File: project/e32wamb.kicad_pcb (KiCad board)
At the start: 2 copper layers, 50 x 37 mm, 34 parts, among them J1 2059-302_998-403, J2 Conn_01x04, J3 Conn_01x03, Q1 AO3400, Q2 AO3400, Q3 AO3400, Q4 AO3400, Q5 AO3400, SW1 TS-1187A-B-A-B, U1 AP63203WU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

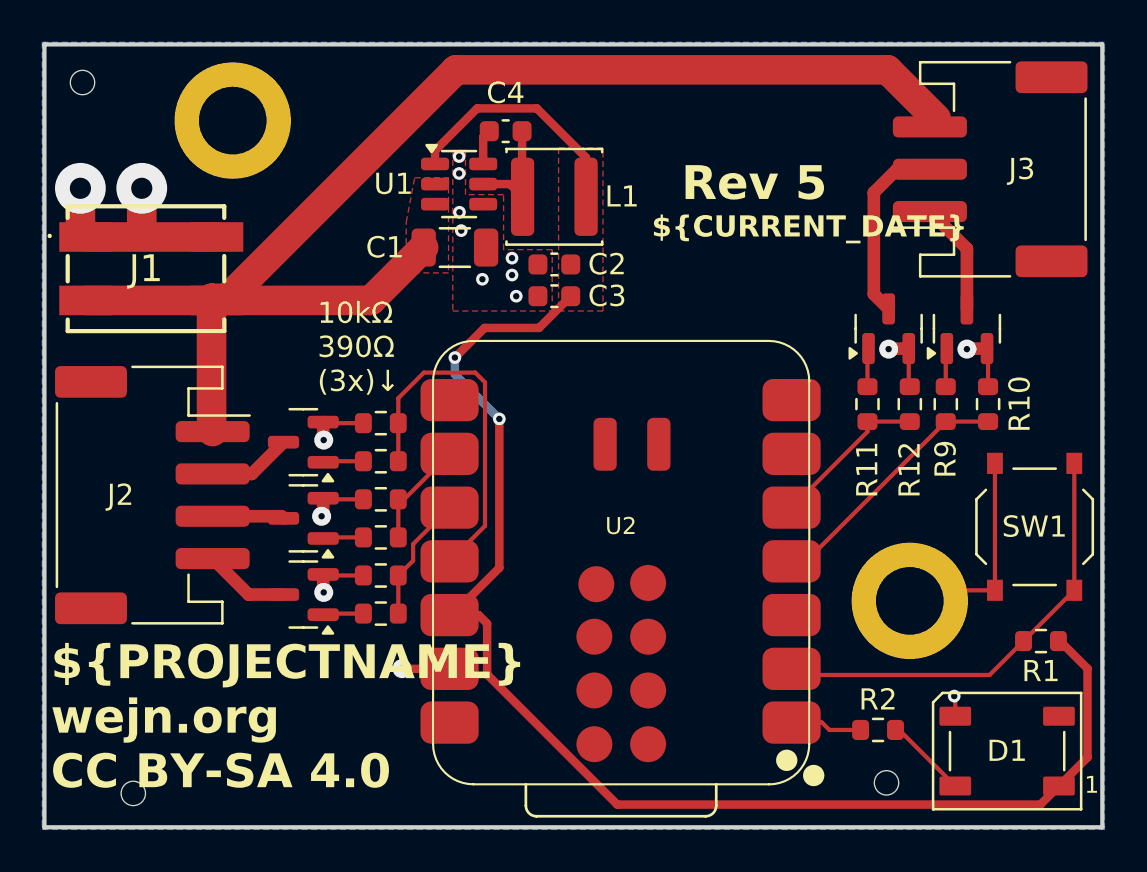
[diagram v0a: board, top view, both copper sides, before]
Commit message: Switch the esp32-c6 to DIP footprint
Sam suggested it might make the debugging a bit easier.
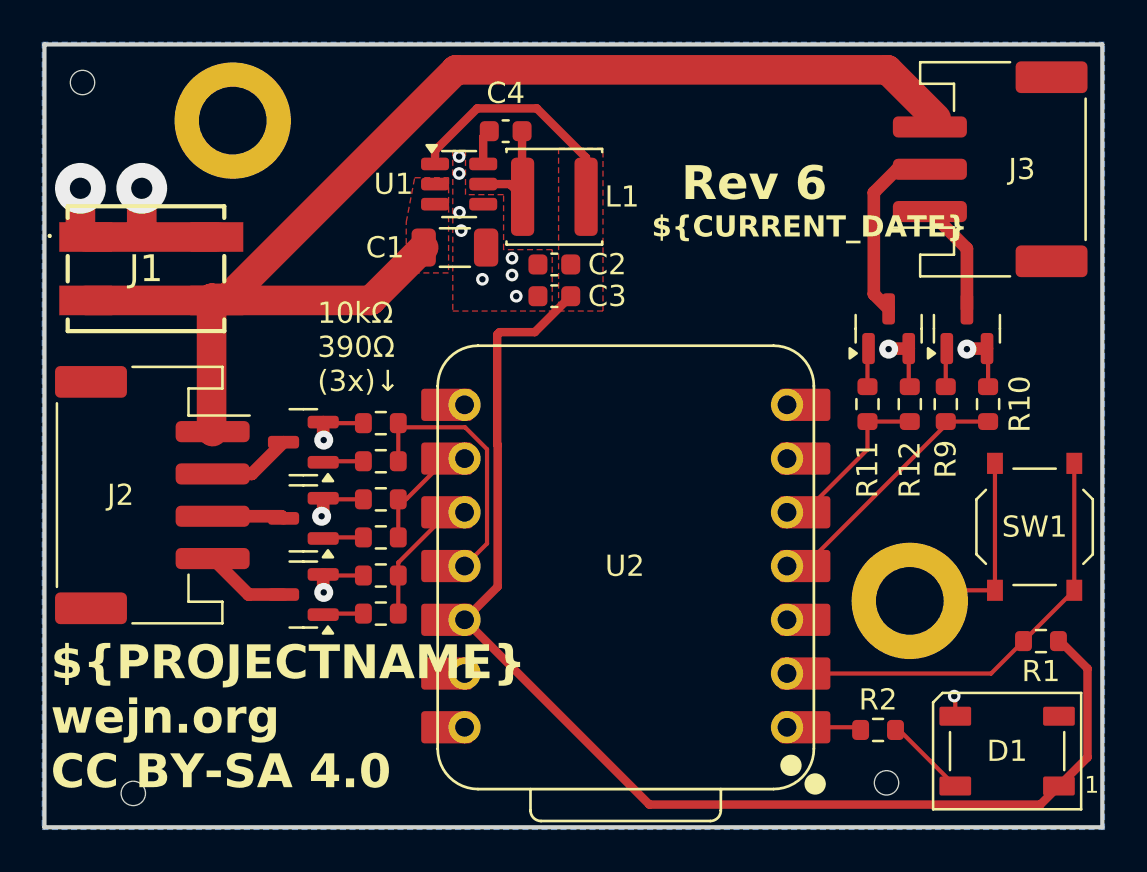
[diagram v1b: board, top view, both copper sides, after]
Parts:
- U2: value XIAO-ESP32-C6-SMD -> XIAO-ESP32-C6-DIP; footprint xiao:XIAO-ESP32C6-SMD -> xiao:XIAO-ESP32C6-DIP
- moved U2 0.45 mm to (77.4, 74.7)
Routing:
- net +3.3V: track 74.1 -> 69.6 mm, vias 2 -> 0
- net pwm drive 0: track 16.9 -> 12.5 mm
- net GND: track 38.7 -> 36.4 mm, vias 17 -> 16
- net status indicator: track 3.41 -> 4.13 mm

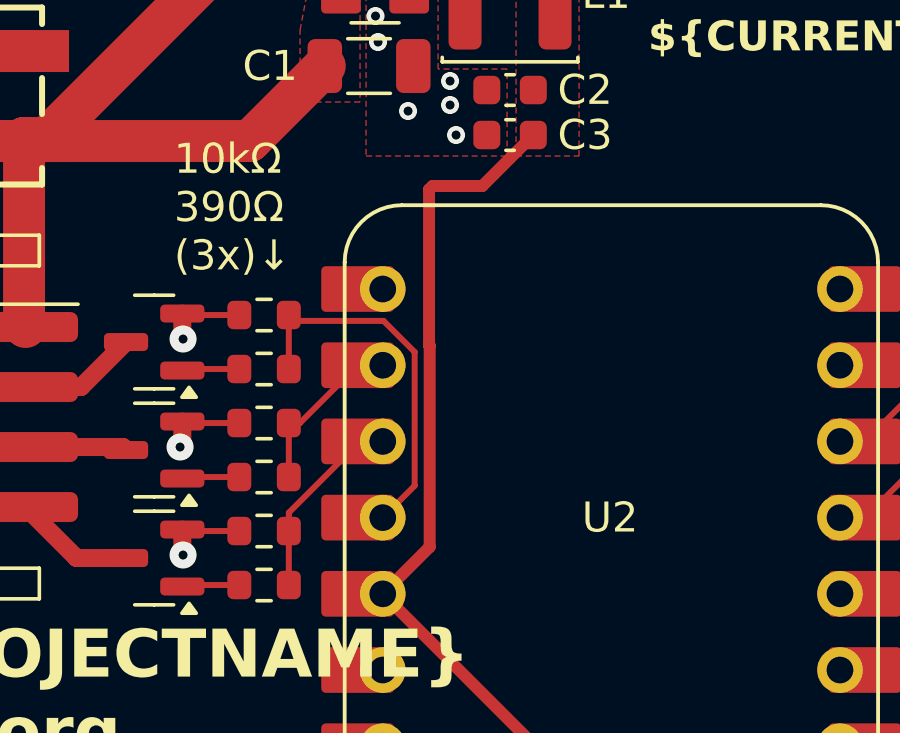
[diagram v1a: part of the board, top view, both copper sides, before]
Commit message: Slightly increase the keepout around antenna
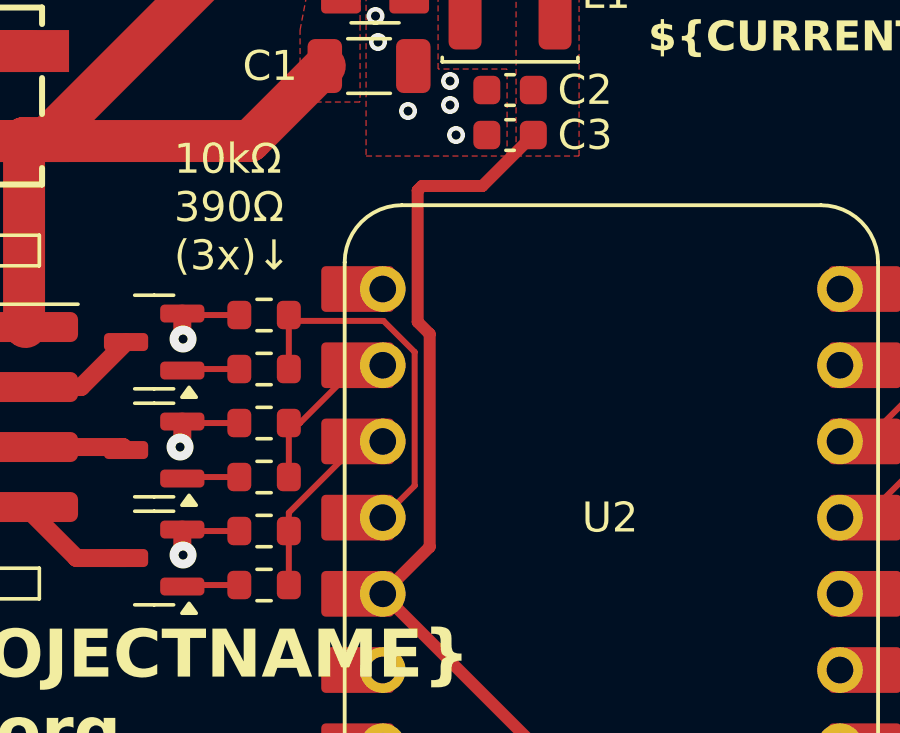
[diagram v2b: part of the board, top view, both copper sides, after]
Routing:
- net +3.3V: track 69.6 -> 70.1 mm
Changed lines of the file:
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@@
+	)
+	(segment
+		(start 71.02 63.745742)
+		(end 71.02 68.129999)
+		(width 0.4)
+		(layer "F.Cu")
+		(net 3)
+	)
+	(segment
+		(start 71.02 68.129999)
+		(end 71.421 68.530999)
+		(width 0.4)
+		(layer "F.Cu")
+		(net 3)
+	)
+	(segment
+		(start 71.166742 63.599)
+		(end 71.02 63.745742)
+		(width 0.4)
+		(layer "F.Cu")
+		(net 3)
 	)
 	(segment
@@
 	)
 	(segment
-		(start 73.176 63.599)
-		(end 71.516742 63.599)
-		(width 0.4)
-		(layer "F.Cu")
-		(net 3)
-	)
-	(segment
-		(start 71.421 68.92537)
+		(start 71.421 68.530999)
 		(end 71.421 75.6292)
 		(width 0.4)
@@
 	)
 	(segment
-		(start 71.516742 63.599)
-		(end 71.4 63.715742)
+		(start 73.176 63.599)
+		(end 71.166742 63.599)
 		(width 0.4)
 		(layer "F.Cu")
@@
 	)
 	(segment
-		(start 71.4 63.715742)
-		(end 71.4 68.904369)
-		(width 0.4)
-		(layer "F.Cu")
-		(net 3)
-	)
-	(segment
 		(start 70.451626 53.024)
 		(end 68.4625 55.013126)
@@
 	)
 	(segment
-		(start 71.4 68.904369)
-		(end 71.421 68.92537)
+		(start 99.3 83.7)
+		(end 97.95 85.05)
 		(width 0.4)
 		(layer "F.Cu")
@@
 		(start 71.421 75.6292)
 		(end 69.857 77.1932)
-		(width 0.4)
-		(layer "F.Cu")
-		(net 3)
-	)
-	(segment
-		(start 99.3 83.7)
-		(end 97.95 85.05)
 		(width 0.4)
 		(layer "F.Cu")
@@
 		(polygon
 			(pts
-				(xy 83.7 63.8) (xy 83.7 66.9) (xy 71.6 66.9) (xy 71.6 63.8)
+				(xy 83.7 63.8) (xy 83.7 66.9) (xy 71.25 66.9) (xy 71.25 63.8)
 			)
 		)

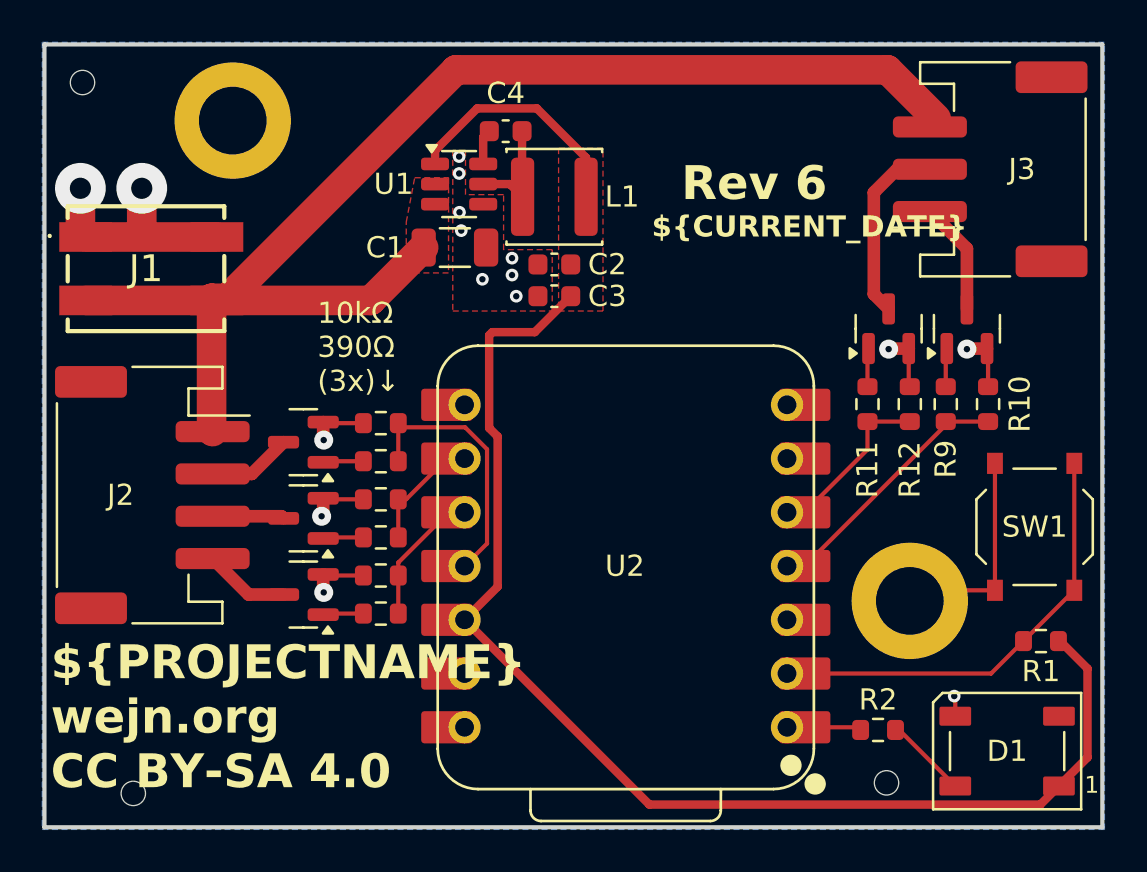
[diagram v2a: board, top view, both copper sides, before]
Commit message: Switch J3 to 4-pin JST PH
Not only will that give me two additional independent chans, but
also one less BOM part to deal with (cheaper for PCBA).
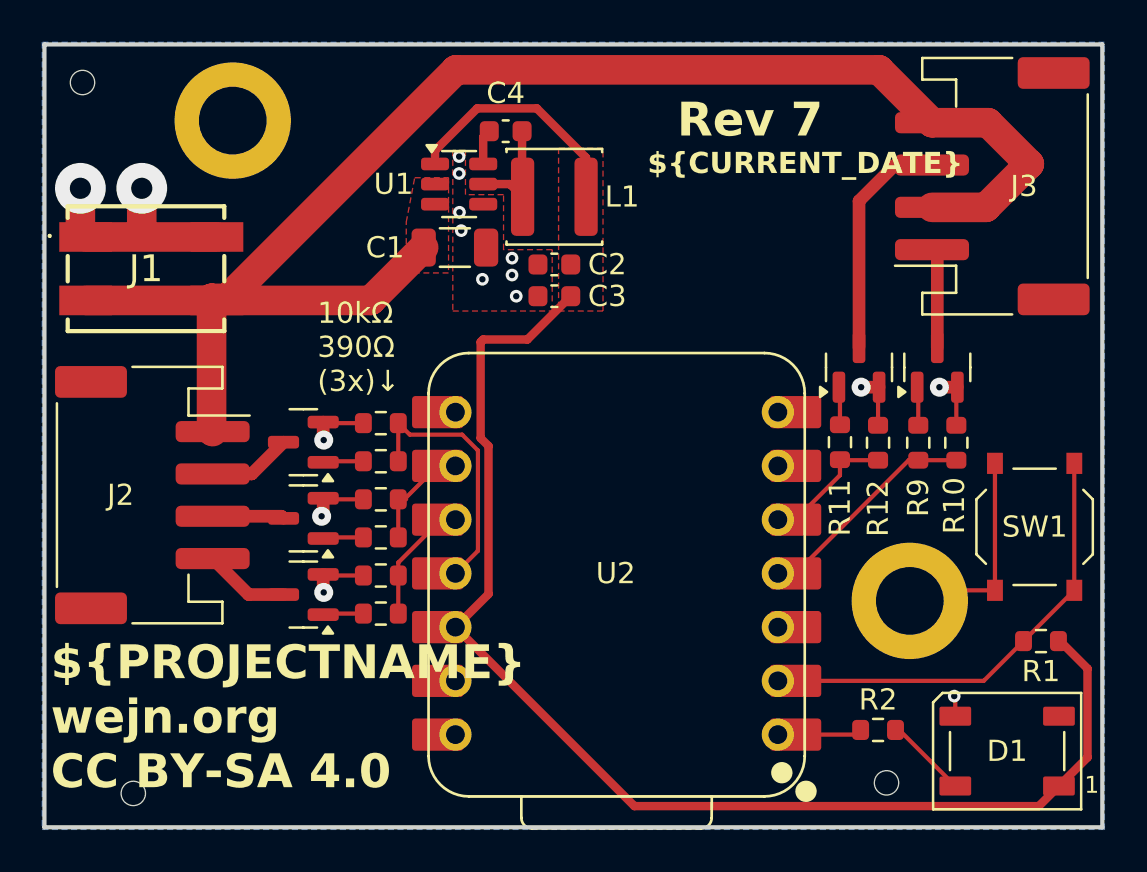
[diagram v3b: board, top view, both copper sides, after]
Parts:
- J3: value Conn_01x03 -> Conn_01x04; footprint misc-lib:JST_PH_S3B-PH-SM4-TB_1x03-1MP_P2.00mm_Horizontal -> misc-lib:JST_PH_S4B-PH-SM4-TB_1x04-1MP_P2.00mm_Horizontal
- moved R10 2.36 mm to (93.1, 68.8)
- moved R12 2.36 mm to (89.4, 68.8)
- moved Q5 2.30 mm to (88.5, 65.3)
- moved Q4 2.30 mm to (92.2, 65.3)
- moved R9 2.24 mm to (91.3, 68.8)
- moved R11 2.22 mm to (87.6, 68.8)
- moved J3 0.81 mm to (94.8, 56.7)
- moved U2 0.55 mm to (77.0, 75.0)
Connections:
- J3 pad 2: led 4 -> VIN
- J3 pad 3: VIN -> led 4
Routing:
- net VIN: track 62.8 -> 73.5 mm
- net led 4: track 8.90 -> 11.1 mm
- net pwm drive 4: track 7.52 -> 5.52 mm
- net pwm drive 3: track 12.3 -> 10.5 mm
- net +3.3V: track 70.1 -> 71.0 mm
- net status indicator: track 4.13 -> 3.35 mm
- net led 3: track 5.32 -> 4.73 mm
- net reset button: track 20.8 -> 21.4 mm
